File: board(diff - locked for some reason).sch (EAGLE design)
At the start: 24 parts, among them IC1 ATMEGA644-20PU, J1 2468, J2 2468, J3 2468, Q1 2N3906, T1 2N3904, T2 2N3904, T3 2N3904, T4 2N3904, U1 MCP1825S-3302E/DB

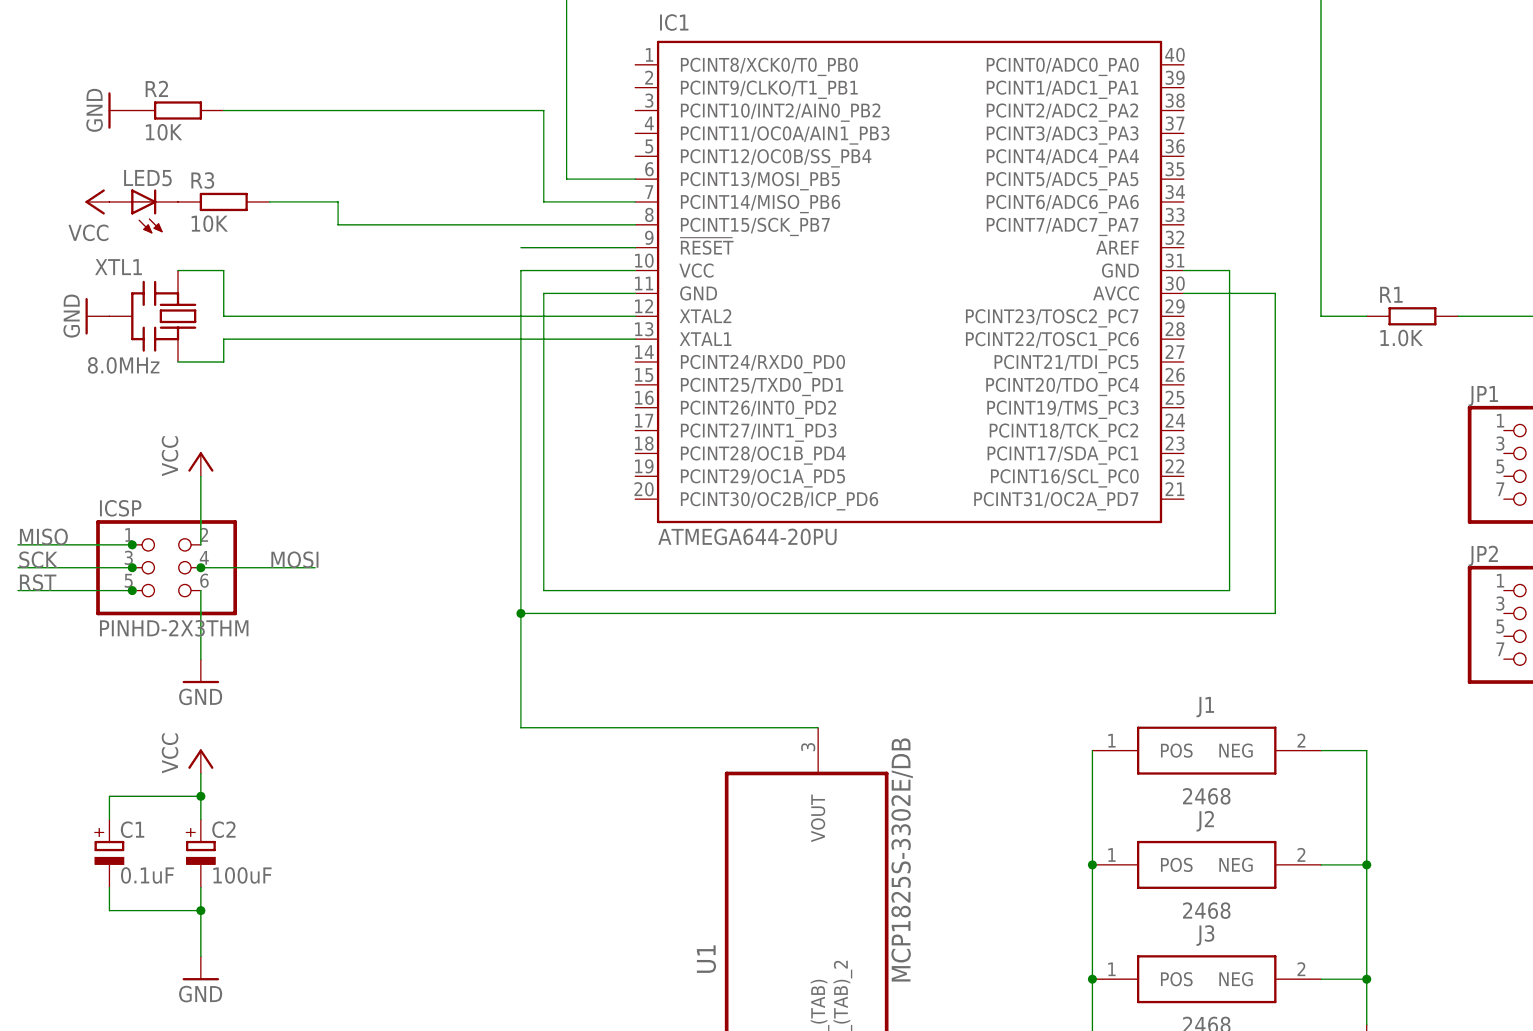
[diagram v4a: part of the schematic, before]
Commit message: modified board to remove extra battery
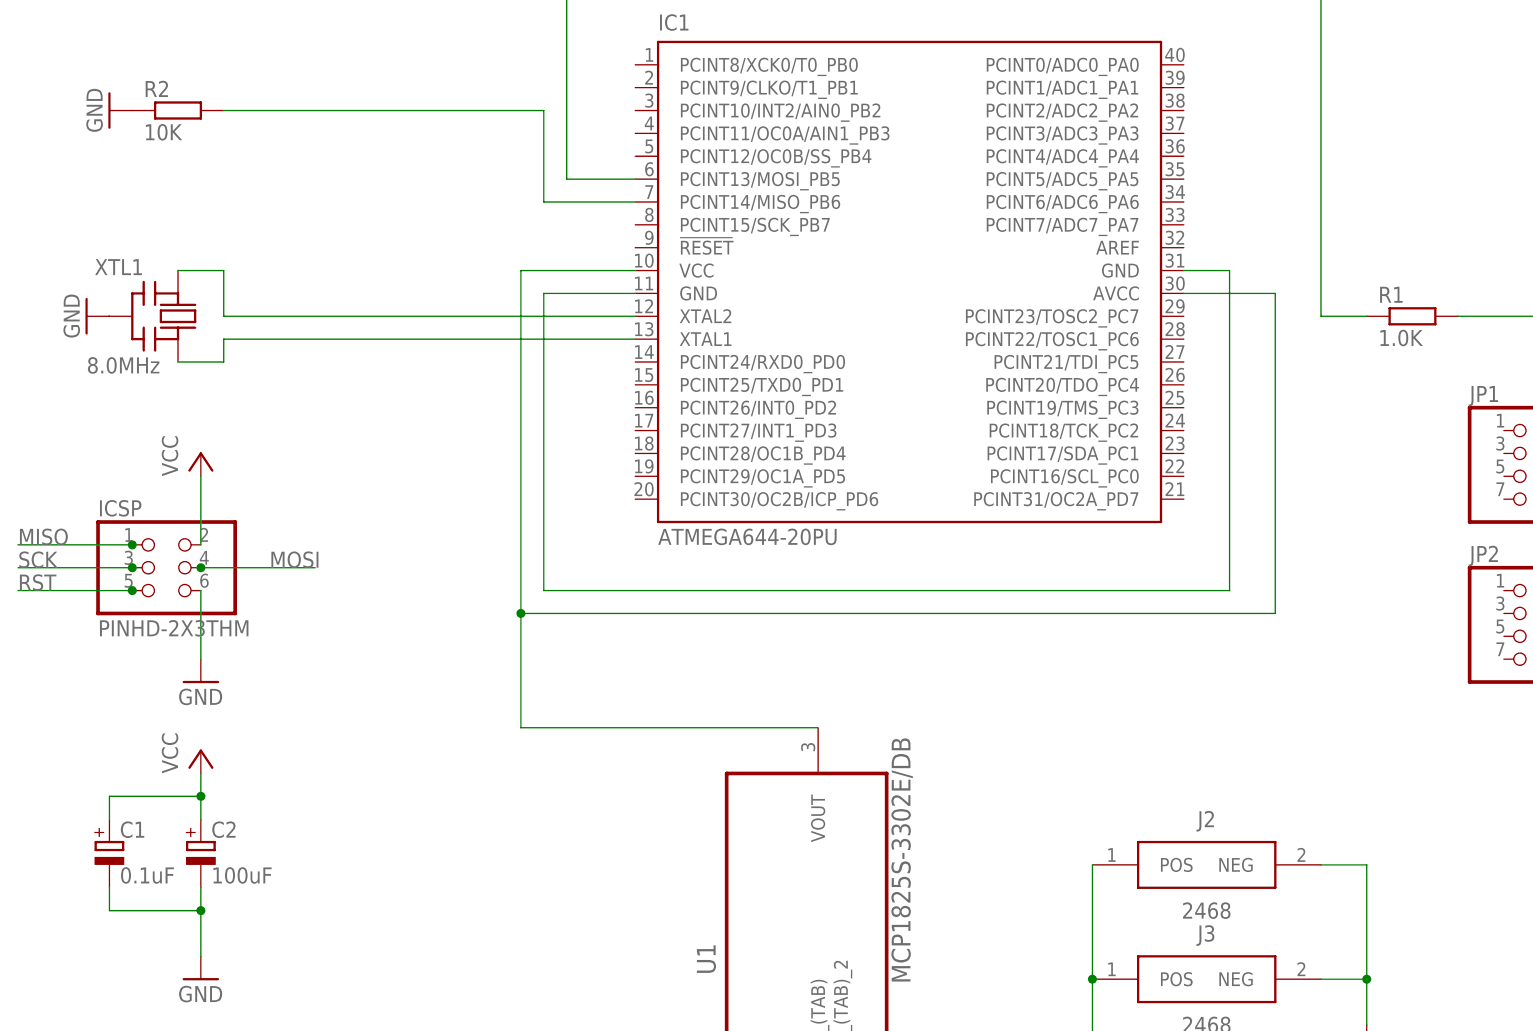
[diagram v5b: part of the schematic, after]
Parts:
- removed J1: 2468, SamacSys_Parts:2468
- removed LED5: (no value), led:LED3MM
- removed R3: 10K, resistor:R-EU_0207/7
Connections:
- removed net N$13: IC1.!RESET
- removed net N$6: LED5.C, R3.1
- removed net N$8: IC1.PCINT15/SCK_PB7, R3.2
- net GND: no longer J1.NEG
- net N$16: no longer J1.POS
- net VCC: no longer LED5.A
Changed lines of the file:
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@@
 <part name="R2" library="resistor" deviceset="R-EU_" device="0207/7" value="10K"/>
 <part name="GND5" library="supply1" deviceset="GND" device=""/>
-<part name="R3" library="resistor" deviceset="R-EU_" device="0207/7" value="10K"/>
-<part name="LED5" library="led" deviceset="LED" device="3MM"/>
-<part name="P+6" library="supply1" deviceset="VCC" device=""/>
 <part name="ICSP" library="adaprog" deviceset="PINHD-2X3" device="THM"/>
 <part name="GND10" library="supply1" deviceset="GND" device=""/>
@@
 <part name="JP1" library="pinhead" library_urn="urn:adsk.eagle:library:325" deviceset="PINHD-2X4" device="" package3d_urn="urn:adsk.eagle:package:22461/2"/>
 <part name="JP2" library="pinhead" library_urn="urn:adsk.eagle:library:325" deviceset="PINHD-2X4" device="" package3d_urn="urn:adsk.eagle:package:22461/2"/>
-<part name="J1" library="SamacSys_Parts" deviceset="2468" device=""/>
 <part name="J2" library="SamacSys_Parts" deviceset="2468" device=""/>
 <part name="J3" library="SamacSys_Parts" deviceset="2468" device=""/>
@@
 <instance part="R2" gate="G$1" x="-142.24" y="109.22"/>
 <instance part="GND5" gate="1" x="-149.86" y="109.22" rot="R270"/>
-<instance part="R3" gate="G$1" x="-137.16" y="99.06"/>
-<instance part="LED5" gate="G$1" x="-147.32" y="99.06" rot="R90"/>
-<instance part="P+6" gate="VCC" x="-152.4" y="99.06" rot="R90"/>
 <instance part="ICSP" gate="G$1" x="-144.78" y="58.42"/>
 <instance part="GND10" gate="1" x="-139.7" y="45.72"/>
@@
 <instance part="JP1" gate="A" x="7.62" y="68.58"/>
 <instance part="JP2" gate="A" x="7.62" y="50.8"/>
-<instance part="J1" gate="G$1" x="-40.64" y="38.1"/>
 <instance part="J2" gate="G$1" x="-40.64" y="25.4"/>
 <instance part="J3" gate="G$1" x="-40.64" y="12.7"/>
@@
 </segment>
 <segment>
-<pinref part="J1" gate="G$1" pin="NEG"/>
-<wire x1="-15.24" y1="38.1" x2="-10.16" y2="38.1" width="0.1524" layer="91"/>
-<wire x1="-10.16" y1="38.1" x2="-10.16" y2="25.4" width="0.1524" layer="91"/>
 <pinref part="J3" gate="G$1" pin="NEG"/>
 <wire x1="-10.16" y1="25.4" x2="-10.16" y2="12.7" width="0.1524" layer="91"/>
@@
 <pinref part="J2" gate="G$1" pin="NEG"/>
 <wire x1="-15.24" y1="25.4" x2="-10.16" y2="25.4" width="0.1524" layer="91"/>
-<junction x="-10.16" y="25.4"/>
 <wire x1="-10.16" y1="12.7" x2="-10.16" y2="7.62" width="0.1524" layer="91"/>
 <junction x="-10.16" y="12.7"/>
@@
 <pinref part="P+5" gate="VCC" pin="VCC"/>
 <wire x1="25.4" y1="101.6" x2="25.4" y2="91.44" width="0.1524" layer="91"/>
-</segment>
-<segment>
-<pinref part="LED5" gate="G$1" pin="A"/>
-<pinref part="P+6" gate="VCC" pin="VCC"/>
 </segment>
 <segment>
@@
 </segment>
 </net>
-<net name="N$8" class="0">
-<segment>
-<pinref part="IC1" gate="G$1" pin="PCINT15/SCK_PB7"/>
-<wire x1="-91.44" y1="96.52" x2="-124.46" y2="96.52" width="0.1524" layer="91"/>
-<wire x1="-124.46" y1="96.52" x2="-124.46" y2="99.06" width="0.1524" layer="91"/>
-<pinref part="R3" gate="G$1" pin="2"/>
-<wire x1="-124.46" y1="99.06" x2="-132.08" y2="99.06" width="0.1524" layer="91"/>
-</segment>
-</net>
-<net name="N$6" class="0">
-<segment>
-<pinref part="R3" gate="G$1" pin="1"/>
-<pinref part="LED5" gate="G$1" pin="C"/>
-</segment>
-</net>
 <net name="SCK" class="0">
 <segment>
@@
 </segment>
 </net>
-<net name="N$13" class="0">
-<segment>
-<pinref part="IC1" gate="G$1" pin="!RESET"/>
-<wire x1="-91.44" y1="93.98" x2="-104.14" y2="93.98" width="0.1524" layer="91"/>
-</segment>
-</net>
 <net name="N$1" class="0">
 <segment>
@@
 <net name="N$16" class="0">
 <segment>
-<pinref part="J1" gate="G$1" pin="POS"/>
 <pinref part="J2" gate="G$1" pin="POS"/>
-<wire x1="-40.64" y1="38.1" x2="-40.64" y2="25.4" width="0.1524" layer="91"/>
 <pinref part="J3" gate="G$1" pin="POS"/>
 <wire x1="-40.64" y1="12.7" x2="-40.64" y2="25.4" width="0.1524" layer="91"/>
-<junction x="-40.64" y="25.4"/>
 <wire x1="-40.64" y1="12.7" x2="-40.64" y2="-10.16" width="0.1524" layer="91"/>
 <junction x="-40.64" y="12.7"/>

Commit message: modified board
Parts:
- removed JP1, JP2: (no value), pinhead:PINHD-2X4
- added SV1, SV2: (no value), con-lstb:MA05-2
- added U2: PEC11R-4015F-S0024, SamacSys_Parts:PEC11R-4015F-S0024
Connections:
- removed net N$7: Q1.B, R1.2
- new net N$21: IC1.PCINT31/OC2A_PD7
- new net N$22: Q1.B, R1.1
- new net PA0: IC1.PCINT0/ADC0_PA0, SV1.8
- new net PA1: IC1.PCINT1/ADC1_PA1, SV1.6
- new net PA2: IC1.PCINT2/ADC2_PA2, SV1.4
- new net PA3: IC1.PCINT3/ADC3_PA3, SV1.2
- new net PA4: IC1.PCINT4/ADC4_PA4, SV1.1
- new net PA5: IC1.PCINT5/ADC5_PA5, SV1.3
- new net PA6: IC1.PCINT6/ADC6_PA6, SV1.5
- new net PA7: IC1.PCINT7/ADC7_PA7, SV1.7
- new net PC0: IC1.PCINT16/SCL_PC0, SV2.8
- new net PC1: IC1.PCINT17/SDA_PC1, SV2.6
- new net PC2: IC1.PCINT18/TCK_PC2, SV2.4
- new net PC3: IC1.PCINT19/TMS_PC3, SV2.2
- new net PC4: IC1.PCINT20/TDO_PC4, SV2.1
- new net PC5: IC1.PCINT21/TDI_PC5, SV2.3
- new net PC6: IC1.PCINT22/TOSC1_PC6, SV2.5
- new net PC7: IC1.PCINT23/TOSC2_PC7, SV2.7
- net GND: now also SV1.9, SV2.9
- net MOSI: now also R1.2; no longer R1.1
- net VCC: now also SV1.10, SV2.10
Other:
- moved on the sheet: LED3, LED6, LED8, LED9, Q1, R1, T1, T2, T3, T4

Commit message: modified board
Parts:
- R2: value 10K -> 10.0K
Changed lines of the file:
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@@
 <?xml version="1.0" encoding="utf-8"?>
 <!DOCTYPE eagle SYSTEM "eagle.dtd">
-<eagle version="8.3.1">
+<eagle version="8.4.1">
 <drawing>
 <settings>
@@
 <part name="P+5" library="supply1" deviceset="VCC" device=""/>
 <part name="R1" library="resistor" deviceset="R-EU_" device="0207/7" value="1.0K"/>
-<part name="R2" library="resistor" deviceset="R-EU_" device="0207/7" value="10K"/>
+<part name="R2" library="resistor" deviceset="R-EU_" device="0207/7" value="10.0K"/>
 <part name="GND5" library="supply1" deviceset="GND" device=""/>
 <part name="ICSP" library="adaprog" deviceset="PINHD-2X3" device="THM"/>

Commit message: finished connections on schematic
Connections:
- removed net N$12: IC1.GND, IC1.GND@1
- removed net N$14: IC1.AVCC, IC1.VCC, U1.VOUT
- new net N$13: IC1.PCINT26/INT0_PD2, U2.1
- new net N$6: IC1.PCINT24/RXD0_PD0, U2.A
- new net N$7: IC1.PCINT25/TXD0_PD1, U2.B
- new net N$8: IC1.AREF, IC1.AVCC, IC1.VCC, U1.VOUT, U2.C
- net N$21: now also IC1.GND, IC1.GND@1, IC1.PCINT10/INT2/AIN0_PB2, IC1.PCINT11/OC0A/AIN1_PB3, IC1.PCINT12/OC0B/SS_PB4, IC1.PCINT28/OC1B_PD4, IC1.PCINT29/OC1A_PD5, IC1.PCINT30/OC2B/ICP_PD6, IC1.PCINT8/XCK0/T0_PB0, IC1.PCINT9/CLKO/T1_PB1, U2.2
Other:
- moved on the sheet: U2
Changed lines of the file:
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@@
 <?xml version="1.0" encoding="utf-8"?>
 <!DOCTYPE eagle SYSTEM "eagle.dtd">
-<eagle version="8.4.1">
+<eagle version="8.3.1">
 <drawing>
 <settings>
@@
 <instance part="J3" gate="G$1" x="-40.64" y="12.7"/>
 <instance part="GND9" gate="1" x="-10.16" y="5.08"/>
-<instance part="U2" gate="G$1" x="0" y="60.96"/>
+<instance part="U2" gate="G$1" x="-129.54" y="48.26"/>
 <instance part="SV1" gate="G$1" x="10.16" y="111.76"/>
 <instance part="SV2" gate="G$1" x="10.16" y="83.82"/>
@@
 </segment>
 </net>
-<net name="N$12" class="0">
-<segment>
-<pinref part="IC1" gate="G$1" pin="GND"/>
-<wire x1="-91.44" y1="88.9" x2="-101.6" y2="88.9" width="0.1524" layer="91"/>
-<wire x1="-101.6" y1="88.9" x2="-101.6" y2="55.88" width="0.1524" layer="91"/>
-<wire x1="-101.6" y1="55.88" x2="-25.4" y2="55.88" width="0.1524" layer="91"/>
-<pinref part="IC1" gate="G$1" pin="GND@1"/>
-<wire x1="-30.48" y1="91.44" x2="-25.4" y2="91.44" width="0.1524" layer="91"/>
-<wire x1="-25.4" y1="91.44" x2="-25.4" y2="55.88" width="0.1524" layer="91"/>
-</segment>
-</net>
-<net name="N$14" class="0">
-<segment>
-<pinref part="IC1" gate="G$1" pin="VCC"/>
-<wire x1="-91.44" y1="91.44" x2="-104.14" y2="91.44" width="0.1524" layer="91"/>
-<wire x1="-104.14" y1="91.44" x2="-104.14" y2="53.34" width="0.1524" layer="91"/>
-<pinref part="IC1" gate="G$1" pin="AVCC"/>
-<wire x1="-30.48" y1="88.9" x2="-20.32" y2="88.9" width="0.1524" layer="91"/>
-<wire x1="-20.32" y1="88.9" x2="-20.32" y2="53.34" width="0.1524" layer="91"/>
-<wire x1="-20.32" y1="53.34" x2="-104.14" y2="53.34" width="0.1524" layer="91"/>
-<pinref part="U1" gate="A" pin="VOUT"/>
-<wire x1="-71.12" y1="40.64" x2="-104.14" y2="40.64" width="0.1524" layer="91"/>
-<wire x1="-104.14" y1="40.64" x2="-104.14" y2="53.34" width="0.1524" layer="91"/>
-<junction x="-104.14" y="53.34"/>
-</segment>
-</net>
 <net name="N$1" class="0">
 <segment>
@@
 <pinref part="IC1" gate="G$1" pin="PCINT31/OC2A_PD7"/>
 <wire x1="-30.48" y1="66.04" x2="-27.94" y2="66.04" width="0.1524" layer="91"/>
+<wire x1="-27.94" y1="66.04" x2="-27.94" y2="58.42" width="0.1524" layer="91"/>
+<pinref part="IC1" gate="G$1" pin="GND"/>
+<wire x1="-91.44" y1="88.9" x2="-96.52" y2="88.9" width="0.1524" layer="91"/>
+<wire x1="-96.52" y1="88.9" x2="-101.6" y2="88.9" width="0.1524" layer="91"/>
+<wire x1="-101.6" y1="88.9" x2="-101.6" y2="71.12" width="0.1524" layer="91"/>
+<wire x1="-101.6" y1="71.12" x2="-101.6" y2="68.58" width="0.1524" layer="91"/>
+<wire x1="-101.6" y1="68.58" x2="-101.6" y2="66.04" width="0.1524" layer="91"/>
+<wire x1="-101.6" y1="66.04" x2="-101.6" y2="58.42" width="0.1524" layer="91"/>
+<wire x1="-101.6" y1="58.42" x2="-101.6" y2="55.88" width="0.1524" layer="91"/>
+<wire x1="-101.6" y1="55.88" x2="-25.4" y2="55.88" width="0.1524" layer="91"/>
+<pinref part="IC1" gate="G$1" pin="GND@1"/>
+<wire x1="-30.48" y1="91.44" x2="-25.4" y2="91.44" width="0.1524" layer="91"/>
+<wire x1="-25.4" y1="91.44" x2="-25.4" y2="55.88" width="0.1524" layer="91"/>
+<pinref part="U2" gate="G$1" pin="2"/>
+<wire x1="-109.22" y1="45.72" x2="-101.6" y2="45.72" width="0.1524" layer="91"/>
+<wire x1="-101.6" y1="45.72" x2="-101.6" y2="55.88" width="0.1524" layer="91"/>
+<junction x="-101.6" y="55.88"/>
+<pinref part="IC1" gate="G$1" pin="PCINT28/OC1B_PD4"/>
+<wire x1="-91.44" y1="71.12" x2="-101.6" y2="71.12" width="0.1524" layer="91"/>
+<junction x="-101.6" y="71.12"/>
+<pinref part="IC1" gate="G$1" pin="PCINT29/OC1A_PD5"/>
+<wire x1="-91.44" y1="68.58" x2="-101.6" y2="68.58" width="0.1524" layer="91"/>
+<junction x="-101.6" y="68.58"/>
+<pinref part="IC1" gate="G$1" pin="PCINT30/OC2B/ICP_PD6"/>
+<wire x1="-91.44" y1="66.04" x2="-101.6" y2="66.04" width="0.1524" layer="91"/>
+<junction x="-101.6" y="66.04"/>
+<pinref part="IC1" gate="G$1" pin="PCINT12/OC0B/SS_PB4"/>
+<wire x1="-91.44" y1="104.14" x2="-96.52" y2="104.14" width="0.1524" layer="91"/>
+<wire x1="-96.52" y1="104.14" x2="-96.52" y2="88.9" width="0.1524" layer="91"/>
+<junction x="-96.52" y="88.9"/>
+<pinref part="IC1" gate="G$1" pin="PCINT11/OC0A/AIN1_PB3"/>
+<wire x1="-91.44" y1="106.68" x2="-96.52" y2="106.68" width="0.1524" layer="91"/>
+<wire x1="-96.52" y1="106.68" x2="-96.52" y2="104.14" width="0.1524" layer="91"/>
+<junction x="-96.52" y="104.14"/>
+<pinref part="IC1" gate="G$1" pin="PCINT10/INT2/AIN0_PB2"/>
+<wire x1="-91.44" y1="109.22" x2="-96.52" y2="109.22" width="0.1524" layer="91"/>
+<wire x1="-96.52" y1="109.22" x2="-96.52" y2="106.68" width="0.1524" layer="91"/>
+<junction x="-96.52" y="106.68"/>
+<pinref part="IC1" gate="G$1" pin="PCINT9/CLKO/T1_PB1"/>
+<wire x1="-91.44" y1="111.76" x2="-96.52" y2="111.76" width="0.1524" layer="91"/>
+<wire x1="-96.52" y1="111.76" x2="-96.52" y2="109.22" width="0.1524" layer="91"/>
+<junction x="-96.52" y="109.22"/>
+<pinref part="IC1" gate="G$1" pin="PCINT8/XCK0/T0_PB0"/>
+<wire x1="-91.44" y1="114.3" x2="-96.52" y2="114.3" width="0.1524" layer="91"/>
+<wire x1="-96.52" y1="114.3" x2="-96.52" y2="111.76" width="0.1524" layer="91"/>
+<junction x="-96.52" y="111.76"/>
+<wire x1="-27.94" y1="58.42" x2="-101.6" y2="58.42" width="0.1524" layer="91"/>
+<junction x="-101.6" y="58.42"/>
 </segment>
 </net>
@@
 </segment>
 </net>
+<net name="N$6" class="0">
+<segment>
+<pinref part="U2" gate="G$1" pin="A"/>
+<wire x1="-129.54" y1="48.26" x2="-132.08" y2="48.26" width="0.1524" layer="91"/>
+<wire x1="-132.08" y1="48.26" x2="-132.08" y2="55.88" width="0.1524" layer="91"/>
+<wire x1="-132.08" y1="55.88" x2="-109.22" y2="55.88" width="0.1524" layer="91"/>
+<wire x1="-109.22" y1="55.88" x2="-109.22" y2="81.28" width="0.1524" layer="91"/>
+<pinref part="IC1" gate="G$1" pin="PCINT24/RXD0_PD0"/>
+<wire x1="-109.22" y1="81.28" x2="-91.44" y2="81.28" width="0.1524" layer="91"/>
+</segment>
+</net>
+<net name="N$7" class="0">
+<segment>
+<pinref part="U2" gate="G$1" pin="B"/>
+<wire x1="-129.54" y1="45.72" x2="-134.62" y2="45.72" width="0.1524" layer="91"/>
+<wire x1="-134.62" y1="45.72" x2="-134.62" y2="30.48" width="0.1524" layer="91"/>
+<wire x1="-134.62" y1="30.48" x2="-106.68" y2="30.48" width="0.1524" layer="91"/>
+<wire x1="-106.68" y1="30.48" x2="-106.68" y2="78.74" width="0.1524" layer="91"/>
+<pinref part="IC1" gate="G$1" pin="PCINT25/TXD0_PD1"/>
+<wire x1="-106.68" y1="78.74" x2="-91.44" y2="78.74" width="0.1524" layer="91"/>
+</segment>
+</net>
+<net name="N$13" class="0">
+<segment>
+<pinref part="U2" gate="G$1" pin="1"/>
+<wire x1="-109.22" y1="48.26" x2="-99.06" y2="48.26" width="0.1524" layer="91"/>
+<wire x1="-99.06" y1="48.26" x2="-99.06" y2="76.2" width="0.1524" layer="91"/>
+<pinref part="IC1" gate="G$1" pin="PCINT26/INT0_PD2"/>
+<wire x1="-99.06" y1="76.2" x2="-91.44" y2="76.2" width="0.1524" layer="91"/>
+</segment>
+</net>
+<net name="N$8" class="0">
+<segment>
+<pinref part="IC1" gate="G$1" pin="AREF"/>
+<wire x1="-30.48" y1="93.98" x2="-17.78" y2="93.98" width="0.1524" layer="91"/>
+<wire x1="-17.78" y1="93.98" x2="-17.78" y2="48.26" width="0.1524" layer="91"/>
+<wire x1="-17.78" y1="48.26" x2="-93.98" y2="48.26" width="0.1524" layer="91"/>
+<wire x1="-93.98" y1="48.26" x2="-93.98" y2="63.5" width="0.1524" layer="91"/>
+<pinref part="IC1" gate="G$1" pin="VCC"/>
+<wire x1="-91.44" y1="91.44" x2="-104.14" y2="91.44" width="0.1524" layer="91"/>
+<wire x1="-104.14" y1="91.44" x2="-104.14" y2="63.5" width="0.1524" layer="91"/>
+<pinref part="IC1" gate="G$1" pin="AVCC"/>
+<wire x1="-104.14" y1="63.5" x2="-104.14" y2="53.34" width="0.1524" layer="91"/>
+<wire x1="-30.48" y1="88.9" x2="-20.32" y2="88.9" width="0.1524" layer="91"/>
+<wire x1="-20.32" y1="88.9" x2="-20.32" y2="53.34" width="0.1524" layer="91"/>
+<wire x1="-20.32" y1="53.34" x2="-104.14" y2="53.34" width="0.1524" layer="91"/>
+<pinref part="U1" gate="A" pin="VOUT"/>
+<wire x1="-71.12" y1="40.64" x2="-104.14" y2="40.64" width="0.1524" layer="91"/>
+<wire x1="-104.14" y1="40.64" x2="-104.14" y2="53.34" width="0.1524" layer="91"/>
+<junction x="-104.14" y="53.34"/>
+<pinref part="U2" gate="G$1" pin="C"/>
+<wire x1="-129.54" y1="43.18" x2="-132.08" y2="43.18" width="0.1524" layer="91"/>
+<wire x1="-132.08" y1="43.18" x2="-132.08" y2="27.94" width="0.1524" layer="91"/>
+<wire x1="-132.08" y1="27.94" x2="-104.14" y2="27.94" width="0.1524" layer="91"/>
+<wire x1="-104.14" y1="27.94" x2="-104.14" y2="40.64" width="0.1524" layer="91"/>
+<junction x="-104.14" y="40.64"/>
+<wire x1="-93.98" y1="63.5" x2="-104.14" y2="63.5" width="0.1524" layer="91"/>
+<junction x="-104.14" y="63.5"/>
+</segment>
+</net>
